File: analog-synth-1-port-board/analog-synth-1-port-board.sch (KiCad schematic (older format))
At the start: 11 parts, among them J1 PJ301M-12, J2 PJ301M-12, J3 Conn_02x08_Odd_Even, J4 PJ301M-12, J5 PJ301M-12, J6 Conn_02x08_Odd_Even

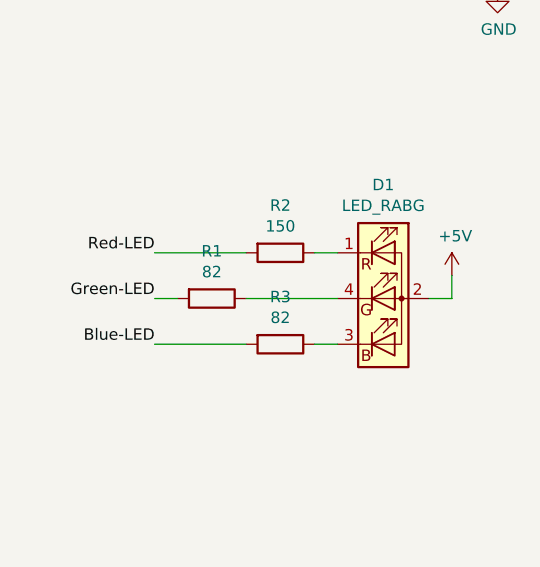
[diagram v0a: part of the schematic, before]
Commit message: Switch from RABG to RCBG LED
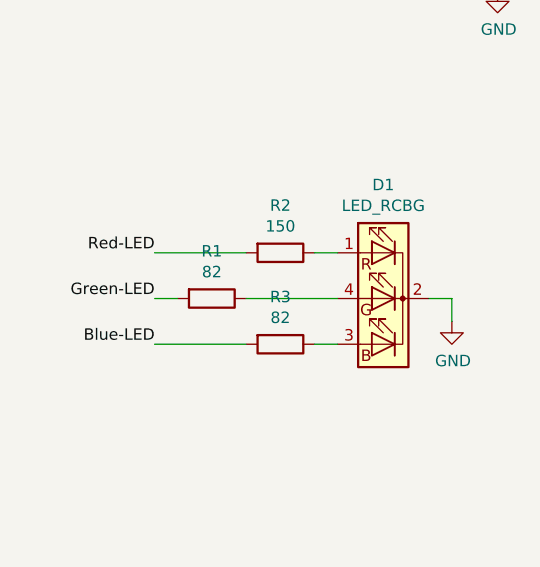
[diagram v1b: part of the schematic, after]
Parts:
- removed D1: LED_RABG, symbol Device:LED_RABG
- added D1: LED_RCBG, symbol Device:LED_RCBG
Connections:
- net GND: now also D1.2 (K)
- net at R2.1: now also D1.1 (RA)
- net at R3.1: now also D1.3 (BA)
- net at R1.1: now also D1.4 (GA)
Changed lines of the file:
@@
 EESchema Schematic File Version 4
+LIBS:analog-synth-1-port-board-cache
 EELAYER 26 0
 EELAYER END
@@
 Connection ~ 8050 2150
 $Comp
-L Device:LED_RABG D1
-U 1 1 5D27CC11
-P 8300 4100
-F 0 "D1" H 8300 4597 50  0000 C CNN
-F 1 "LED_RABG" H 8300 4506 50  0000 C CNN
-F 2 "" H 8300 4050 50  0001 C CNN
-F 3 "~" H 8300 4050 50  0001 C CNN
-	1    8300 4100
-	1    0    0    -1
-$EndComp
-$Comp
 L Device:R R2
 U 1 1 5D27CF30
@@
 	7700 3900 7300 3900
 $Comp
-L power:+5V #PWR08
-U 1 1 5D28128C
-P 8600 4000
-F 0 "#PWR08" H 8600 3850 50  0001 C CNN
-F 1 "+5V" H 8615 4173 50  0000 C CNN
-F 2 "" H 8600 4000 50  0001 C CNN
-F 3 "" H 8600 4000 50  0001 C CNN
-	1    8600 4000
-	1    0    0    -1
-$EndComp
-Wire Wire Line
-	8600 4000 8600 4100
+L Device:LED_RCBG D1
+U 1 1 5D26F8B7
+P 8300 4100
+F 0 "D1" H 8300 4597 50  0000 C CNN
+F 1 "LED_RCBG" H 8300 4506 50  0000 C CNN
+F 2 "" H 8300 4050 50  0001 C CNN
+F 3 "~" H 8300 4050 50  0001 C CNN
+	1    8300 4100
+	-1   0    0    -1
+$EndComp
+$Comp
+L power:GND #PWR?
+U 1 1 5D271F1C
+P 8600 4200
+F 0 "#PWR?" H 8600 3950 50  0001 C CNN
+F 1 "GND" H 8605 4027 50  0000 C CNN
+F 2 "" H 8600 4200 50  0001 C CNN
+F 3 "" H 8600 4200 50  0001 C CNN
+	1    8600 4200
+	1    0    0    -1
+$EndComp
+Wire Wire Line
+	8600 4200 8600 4100
 Wire Wire Line
 	8600 4100 8500 4100

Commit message: Replace PJ301M-12 with PJ398SM
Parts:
- J1, J2, J4, J5: value PJ301M-12 -> PJ398SM; symbol custom-components:PJ301M-12 -> custom-components:PJ398SM
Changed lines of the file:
@@
 Connection ~ 3250 2150
 $Comp
-L custom-components:PJ301M-12 J1
+L custom-components:PJ398SM J1
 U 1 1 5D26D2E3
 P 2050 3950
 F 0 "J1" V 2010 3772 50  0000 R CNN
-F 1 "PJ301M-12" V 2101 3772 50  0000 R CNN
+F 1 "PJ398SM" V 2101 3772 50  0000 R CNN
 F 2 "" H 2050 3950 50  0000 C CNN
 F 3 "" H 2050 3950 50  0000 C CNN
@@
 $EndComp
 $Comp
-L custom-components:PJ301M-12 J4
+L custom-components:PJ398SM J4
 U 1 1 5D26D3D0
 P 3550 3950
 F 0 "J4" V 3510 3772 50  0000 R CNN
-F 1 "PJ301M-12" V 3601 3772 50  0000 R CNN
+F 1 "PJ398SM" V 3601 3772 50  0000 R CNN
 F 2 "" H 3550 3950 50  0000 C CNN
 F 3 "" H 3550 3950 50  0000 C CNN
@@
 $EndComp
 $Comp
-L custom-components:PJ301M-12 J2
+L custom-components:PJ398SM J2
 U 1 1 5D26D4E3
 P 2050 6050
 F 0 "J2" V 2010 5872 50  0000 R CNN
-F 1 "PJ301M-12" V 2101 5872 50  0000 R CNN
+F 1 "PJ398SM" V 2101 5872 50  0000 R CNN
 F 2 "" H 2050 6050 50  0000 C CNN
 F 3 "" H 2050 6050 50  0000 C CNN
@@
 $EndComp
 $Comp
-L custom-components:PJ301M-12 J5
+L custom-components:PJ398SM J5
 U 1 1 5D26D561
 P 3550 6050
 F 0 "J5" V 3510 5872 50  0000 R CNN
-F 1 "PJ301M-12" V 3601 5872 50  0000 R CNN
+F 1 "PJ398SM" V 3601 5872 50  0000 R CNN
 F 2 "" H 3550 6050 50  0000 C CNN
 F 3 "" H 3550 6050 50  0000 C CNN

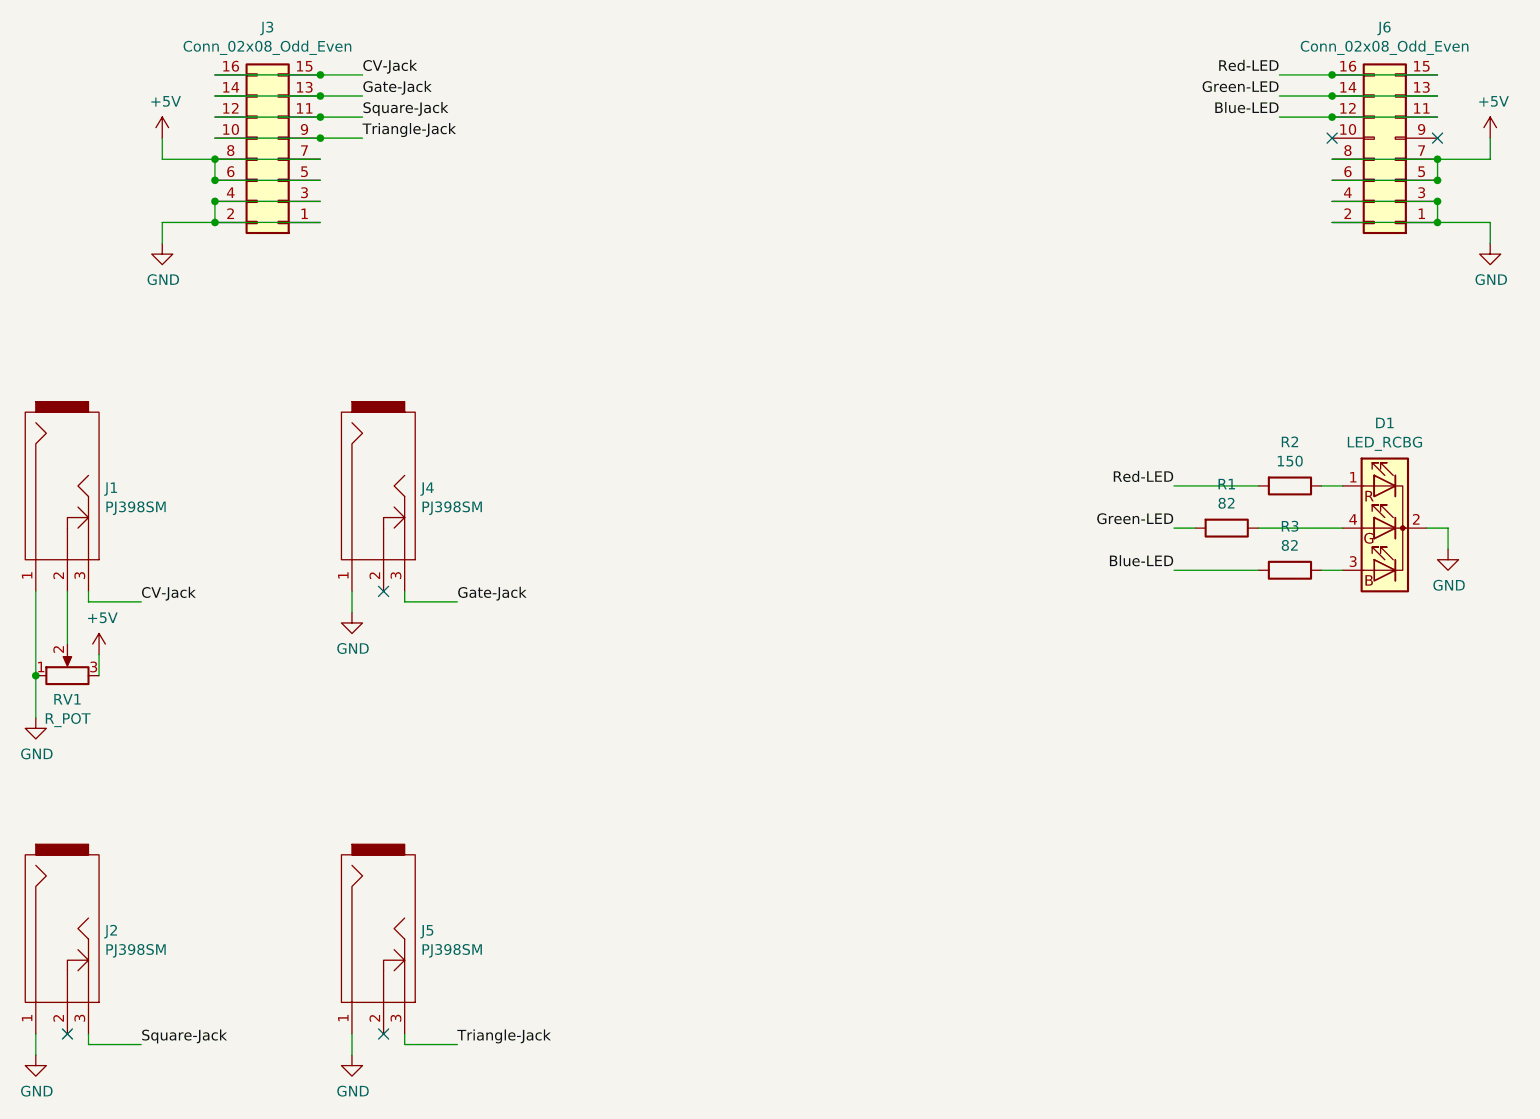
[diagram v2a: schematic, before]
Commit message: Add CV offset & scale system
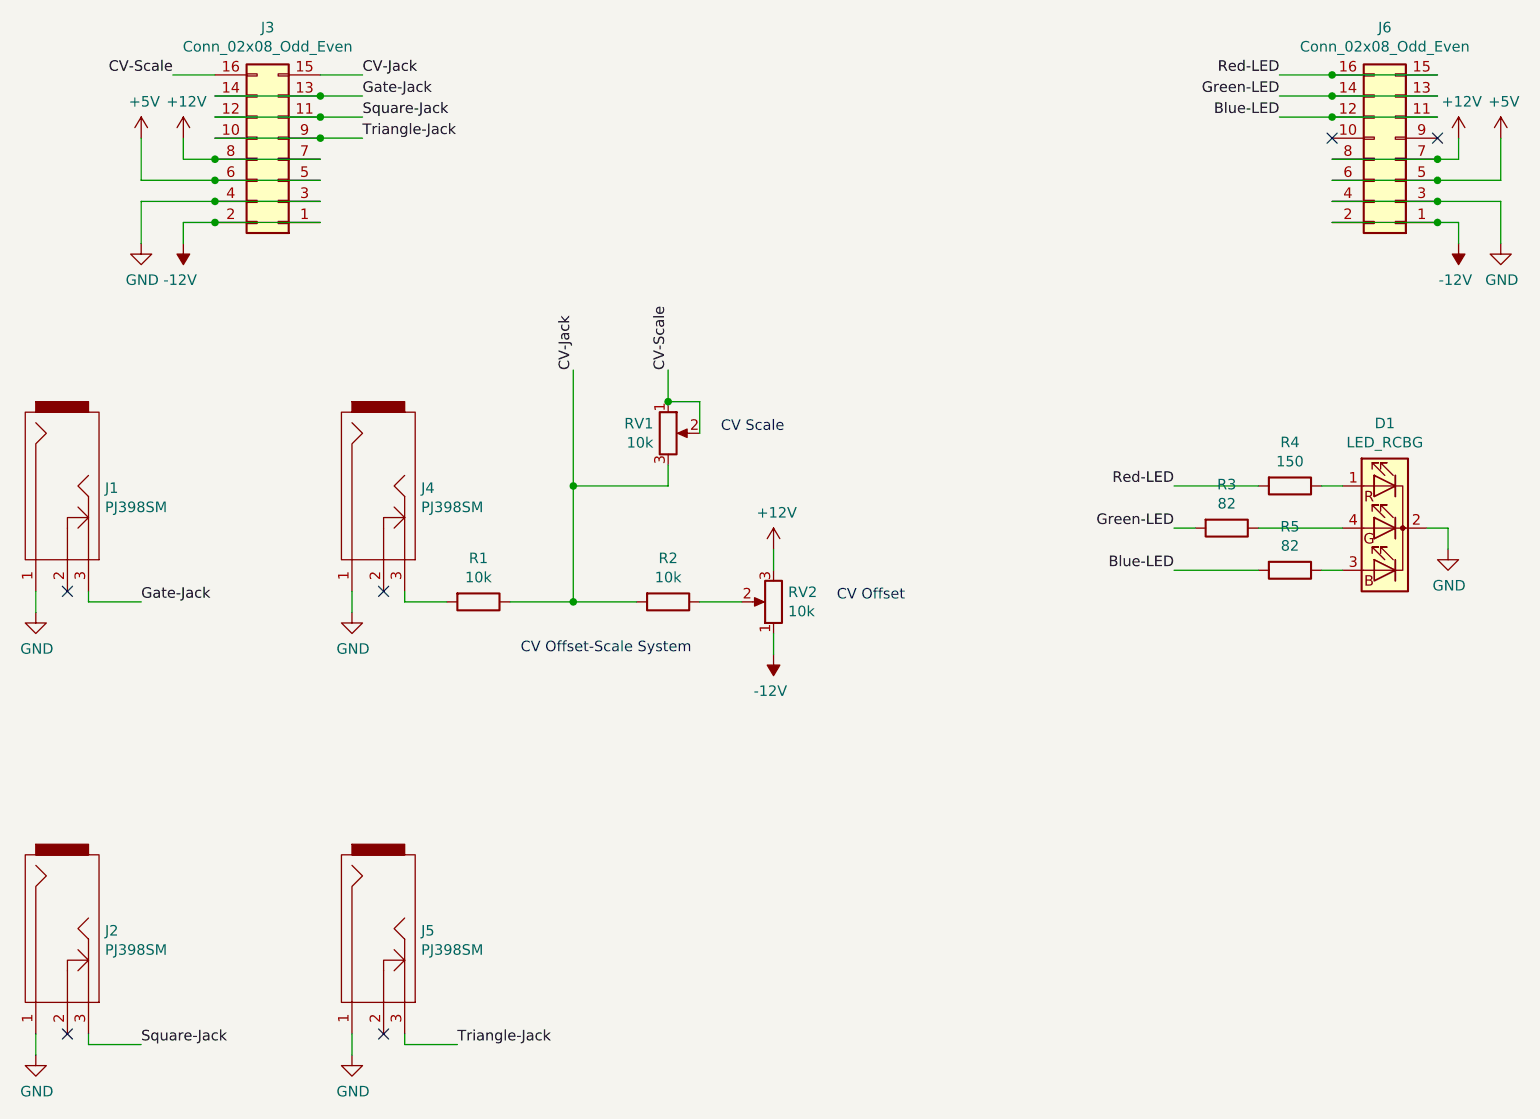
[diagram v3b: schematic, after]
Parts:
- added R1, R2: 10k, symbol Device:R
- added RV2: 10k, symbol Device:R_POT
- RV1: value R_POT -> 10k
- renumbered J4 to J1, J1 to J4, R1 to R3, R2 to R4, R3 to R5
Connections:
- net +5V: no longer J3.7 (Pin_7), J3.8 (Pin_8), J6.7 (Pin_7), J6.8 (Pin_8), RV1.3
- net CV-Jack: now also RV1.3, R1.1, R2.2; no longer J3.16 (Pin_16), J4.3
- net GND: no longer J3.1 (Pin_1), J3.2 (Pin_2), J6.1 (Pin_1), J6.2 (Pin_2), RV1.1
- net at J4.2: no longer RV1.2
- new net: J4.3, R1.2
- new net: R2.1, RV2.2
- new net +12V: J3.7 (Pin_7), J3.8 (Pin_8), J6.7 (Pin_7), J6.8 (Pin_8), RV2.3
- new net -12V: J3.1 (Pin_1), J3.2 (Pin_2), J6.1 (Pin_1), J6.2 (Pin_2), RV2.1
- new net CV-Scale: J3.16 (Pin_16), RV1.1, RV1.2
- no-connect marks 5 -> 6
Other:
- note added: "CV Offset"
- note added: "CV Offset-Scale System"
- note added: "CV Scale"
- moved on the sheet: J1, J4
